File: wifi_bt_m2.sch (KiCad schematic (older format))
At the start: 41 parts, among them J1801 u.FL, J1802 u.FL, J1803 Key_E, Q1801 FDV301N, Q1802 FDV301N, SW1801 WLAN_HKS, U1801 NTB0104GU12, U1802 NTB0104GU12, U1803 74AUP2G08

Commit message: Replace logic gate packages with cheaper options, change associated footprints to ones which match the cheaper alternatives
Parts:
- U1803: value 74AUP2G08 -> 74LVC2G08; footprint dvk-mx8m-bsb:PSOP-08 -> dvk-mx8m-bsb:74LVC2G08DCU; Distrib Link https://store.ti.com/SN74AUP2G08DCUR.aspx -> https://www.rocelec.com/part/textissn74lvc2g08dcu6; Distrib PN 296-32271-1-ND -> SN74LVC2G08DCU6; MFG Part Num SN74AUP2G08DCUR -> SN74LVC2G08DCU; Others https://www.digikey.com/products/en/integrated-circuits-ics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 -> https://store.ti.com/SN74AUP2G08DCUR.aspx
- U1803: value 74AUP2G08 -> 74LVC2G08; footprint dvk-mx8m-bsb:PSOP-08 -> dvk-mx8m-bsb:74LVC2G08DCU; Distrib Link https://store.ti.com/SN74AUP2G08DCUR.aspx -> https://www.rocelec.com/part/textissn74lvc2g08dcu6; Distrib PN 296-32271-1-ND -> SN74AUP2G08DCU6; MFG Part Num SN74AUP2G08DCUR -> SN74AUP2G08DCU; Others https://www.digikey.com/products/en/integrated-circuits-ics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 -> https://store.ti.com/SN74AUP2G08DCUR.aspx
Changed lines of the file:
@@
 P 7550 3550
 F 0 "U1803" H 7550 3600 50  0000 C CNN
-F 1 "74AUP2G08" H 7550 3500 50  0000 C CNN
-F 2 "dvk-mx8m-bsb:PSOP-08" H 7550 3550 50  0001 C CNN
-F 3 "http://www.ti.com/lit/ds/symlink/sn74aup2g08.pdf" H 7550 3550 50  0001 C CNN
+F 1 "74LVC2G08" H 7550 3500 50  0000 C CNN
+F 2 "dvk-mx8m-bsb:74LVC2G08DCU" H 7550 3550 50  0001 C CNN
+F 3 "http://www.ti.com/lit/ds/symlink/sn74lvc2g08.pdf" H 7550 3550 50  0001 C CNN
 F 4 "Texas Instruments" H 7550 3550 60  0001 C CNN "MFG Name"
-F 5 "SN74AUP2G08DCUR" H 7550 3550 60  0001 C CNN "MFG Part Num"
-F 6 "296-32271-1-ND" H 7550 3550 60  0001 C CNN "Distrib PN"
-F 7 "https://store.ti.com/SN74AUP2G08DCUR.aspx" H 7550 3550 60  0001 C CNN "Distrib Link"
+F 5 "SN74LVC2G08DCU" H 7550 3550 60  0001 C CNN "MFG Part Num"
+F 6 "SN74LVC2G08DCU6" H 7550 3550 60  0001 C CNN "Distrib PN"
+F 7 "https://www.rocelec.com/part/textissn74lvc2g08dcu6" H 7550 3550 60  0001 C CNN "Distrib Link"
 F 8 "-" H 7550 3550 60  0001 C CNN "Tolerance"
-F 9 "https://www.digikey.com/products/en/integrated-circuits-ics/logic-gates-and-inverters/705?k=74AUP2G08" H 7550 3550 60  0001 C CNN "Others"
+F 9 "https://store.ti.com/SN74AUP2G08DCUR.aspx" H 7550 3550 60  0001 C CNN "Others"
 	1    7550 3550
 	-1   0    0    -1
@@
 P 7550 4450
 F 0 "U1803" H 7550 4500 50  0000 C CNN
-F 1 "74AUP2G08" H 7550 4400 50  0000 C CNN
-F 2 "dvk-mx8m-bsb:PSOP-08" H 7550 4450 50  0001 C CNN
+F 1 "74LVC2G08" H 7550 4400 50  0000 C CNN
+F 2 "dvk-mx8m-bsb:74LVC2G08DCU" H 7550 4450 50  0001 C CNN
 F 3 "http://www.ti.com/lit/ds/symlink/sn74aup2g08.pdf" H 7550 4450 50  0001 C CNN
 F 4 "Texas Instruments" H 7550 4450 60  0001 C CNN "MFG Name"
-F 5 "SN74AUP2G08DCUR" H 7550 4450 60  0001 C CNN "MFG Part Num"
-F 6 "296-32271-1-ND" H 7550 4450 60  0001 C CNN "Distrib PN"
-F 7 "https://store.ti.com/SN74AUP2G08DCUR.aspx" H 7550 4450 60  0001 C CNN "Distrib Link"
+F 5 "SN74AUP2G08DCU" H 7550 4450 60  0001 C CNN "MFG Part Num"
+F 6 "SN74AUP2G08DCU6" H 7550 4450 60  0001 C CNN "Distrib PN"
+F 7 "https://www.rocelec.com/part/textissn74lvc2g08dcu6" H 7550 4450 60  0001 C CNN "Distrib Link"
 F 8 "-" H 7550 4450 60  0001 C CNN "Tolerance"
-F 9 "https://www.digikey.com/products/en/integrated-circuits-ics/logic-gates-and-inverters/705?k=74AUP2G08" H 7550 4450 60  0001 C CNN "Others"
+F 9 "https://store.ti.com/SN74AUP2G08DCUR.aspx" H 7550 4450 60  0001 C CNN "Others"
 	2    7550 4450
 	-1   0    0    -1

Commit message: Add WLAN+BT antenna component information
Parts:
- AE1801, AE1802: value Antenna -> FR05-S1-NO-1-004
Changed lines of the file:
@@
 P 1700 1800
 F 0 "AE1801" H 1625 1850 50  0000 R CNN
-F 1 "Antenna" H 1625 1775 50  0000 R CNN
+F 1 "FR05-S1-NO-1-004" H 1625 1775 50  0000 R CNN
 F 2 "dvk-mx8m-bsb:placeholder_WLAN+BT_antenna" H 1700 1800 50  0001 C CNN
-F 3 "" H 1700 1800 50  0001 C CNN
+F 3 "https://www.fractusantennas.com/files/UM_FR05_S1_NO_1_004.pdf" H 1700 1800 50  0001 C CNN
 	1    1700 1800
 	1    0    0    -1
@@
 P 1700 2650
 F 0 "AE1802" H 1625 2700 50  0000 R CNN
-F 1 "Antenna" H 1625 2625 50  0000 R CNN
+F 1 "FR05-S1-NO-1-004" H 1625 2625 50  0000 R CNN
 F 2 "dvk-mx8m-bsb:placeholder_WLAN+BT_antenna" H 1700 2650 50  0001 C CNN
-F 3 "" H 1700 2650 50  0001 C CNN
+F 3 "https://www.fractusantennas.com/files/UM_FR05_S1_NO_1_004.pdf" H 1700 2650 50  0001 C CNN
 	1    1700 2650
 	1    0    0    -1

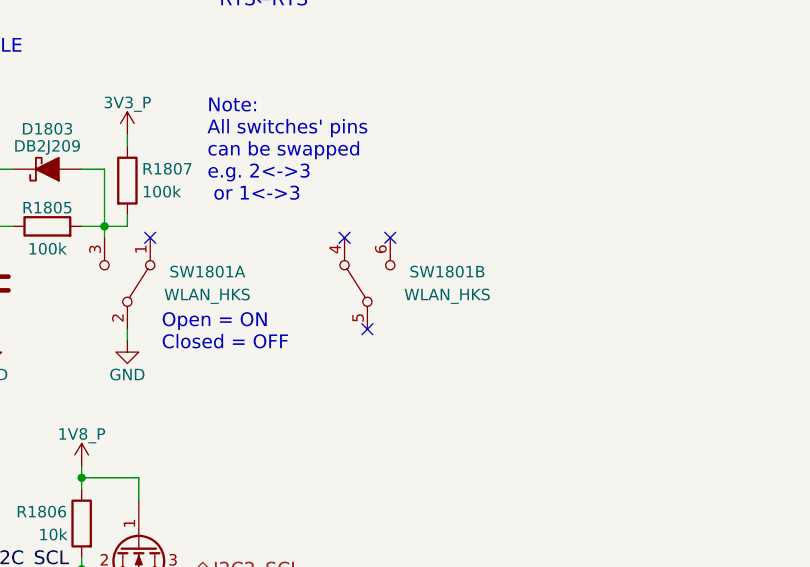
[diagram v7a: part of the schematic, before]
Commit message: Make a few minor aesthetic adjustments to the schematic
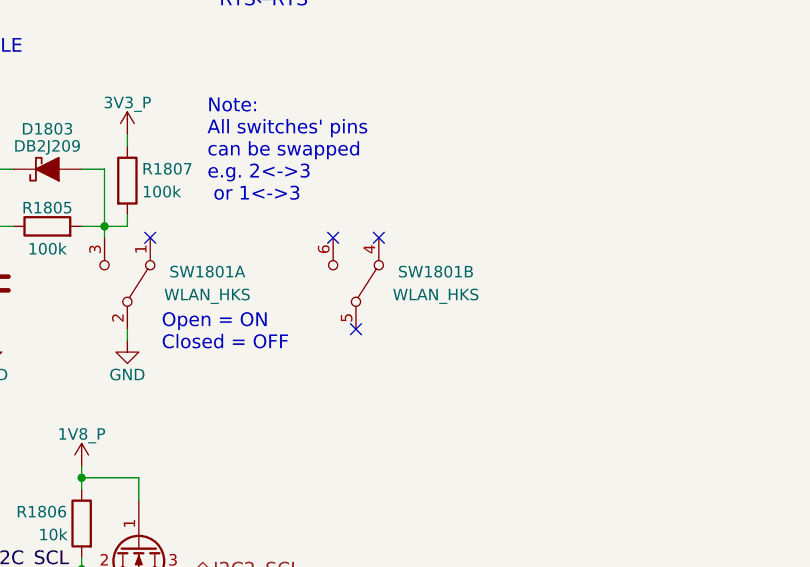
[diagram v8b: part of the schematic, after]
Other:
- moved on the sheet: SW1801B
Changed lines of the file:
@@
 L SW_DPDT_x2 SW1801
 U 2 1 5B1221A9
-P 10650 4250
-F 0 "SW1801" V 10700 3900 50  0000 C CNN
-F 1 "WLAN_HKS" V 10600 3900 50  0000 C CNN
-F 2 "dvk-mx8m-bsb:Switch_CK_DPDT_JS202011JAQN" H 10650 4250 50  0001 C CNN
-F 3 "https://www.ckswitches.com/media/1422/js.pdf" H 10650 4250 50  0001 C CNN
-F 4 "C&K" V 10650 4250 60  0001 C CNN "MFG Name"
-F 5 "JS202011JAQN" V 10650 4250 60  0001 C CNN "MFG Part Num"
-F 6 "CKN10722CT-ND" V 10650 4250 60  0001 C CNN "Distrib PN"
-F 7 "https://www.digikey.com/product-detail/en/c-k/JS202011JAQN/CKN10722CT-ND/6137636" V 10650 4250 60  0001 C CNN "Distrib Link"
-F 8 "-" V 10650 4250 60  0001 C CNN "Tolerance"
-F 9 "https://www.digikey.com/products/en/switches/slide-switches/213?FV=2080004%2Cffe000d5%2C1140003%2C1140160%2C1f140000&quantity=&ColumnSort=1000011&page=1&pageSize=500" V 10650 4250 60  0001 C CNN "Others"
-	2    10650 4250
-	0    -1   -1   0
+P 10600 4250
+F 0 "SW1801" V 10650 4600 50  0000 C CNN
+F 1 "WLAN_HKS" V 10550 4600 50  0000 C CNN
+F 2 "dvk-mx8m-bsb:Switch_CK_DPDT_JS202011JAQN" H 10600 4250 50  0001 C CNN
+F 3 "https://www.ckswitches.com/media/1422/js.pdf" H 10600 4250 50  0001 C CNN
+F 4 "C&K" V 10600 4250 60  0001 C CNN "MFG Name"
+F 5 "JS202011JAQN" V 10600 4250 60  0001 C CNN "MFG Part Num"
+F 6 "CKN10722CT-ND" V 10600 4250 60  0001 C CNN "Distrib PN"
+F 7 "https://www.digikey.com/product-detail/en/c-k/JS202011JAQN/CKN10722CT-ND/6137636" V 10600 4250 60  0001 C CNN "Distrib Link"
+F 8 "-" V 10600 4250 60  0001 C CNN "Tolerance"
+F 9 "https://www.digikey.com/products/en/switches/slide-switches/213?FV=2080004%2Cffe000d5%2C1140003%2C1140160%2C1f140000&quantity=&ColumnSort=1000011&page=1&pageSize=500" V 10600 4250 60  0001 C CNN "Others"
+	2    10600 4250
+	0    1    -1   0
 $EndComp
 NoConn ~ 9700 4050
-NoConn ~ 10550 4050
-NoConn ~ 10750 4050
-NoConn ~ 10650 4450
+NoConn ~ 10500 4050
+NoConn ~ 10700 4050
+NoConn ~ 10600 4450
 NoConn ~ 19750 8050
 $Comp
